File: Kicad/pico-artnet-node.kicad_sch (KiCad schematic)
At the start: 28 parts, among them J1 Conn_01x03_Pin, J2 Conn_01x03_Pin, J3 Conn_01x04_Pin, J4 Conn_01x05_Pin, J5 Conn_01x05_Pin, J6 Conn_01x02_Socket, J7 Conn_01x02_Socket, SW1 SW_SPST, SW2 SW_SPST, SW3 SW_SPST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

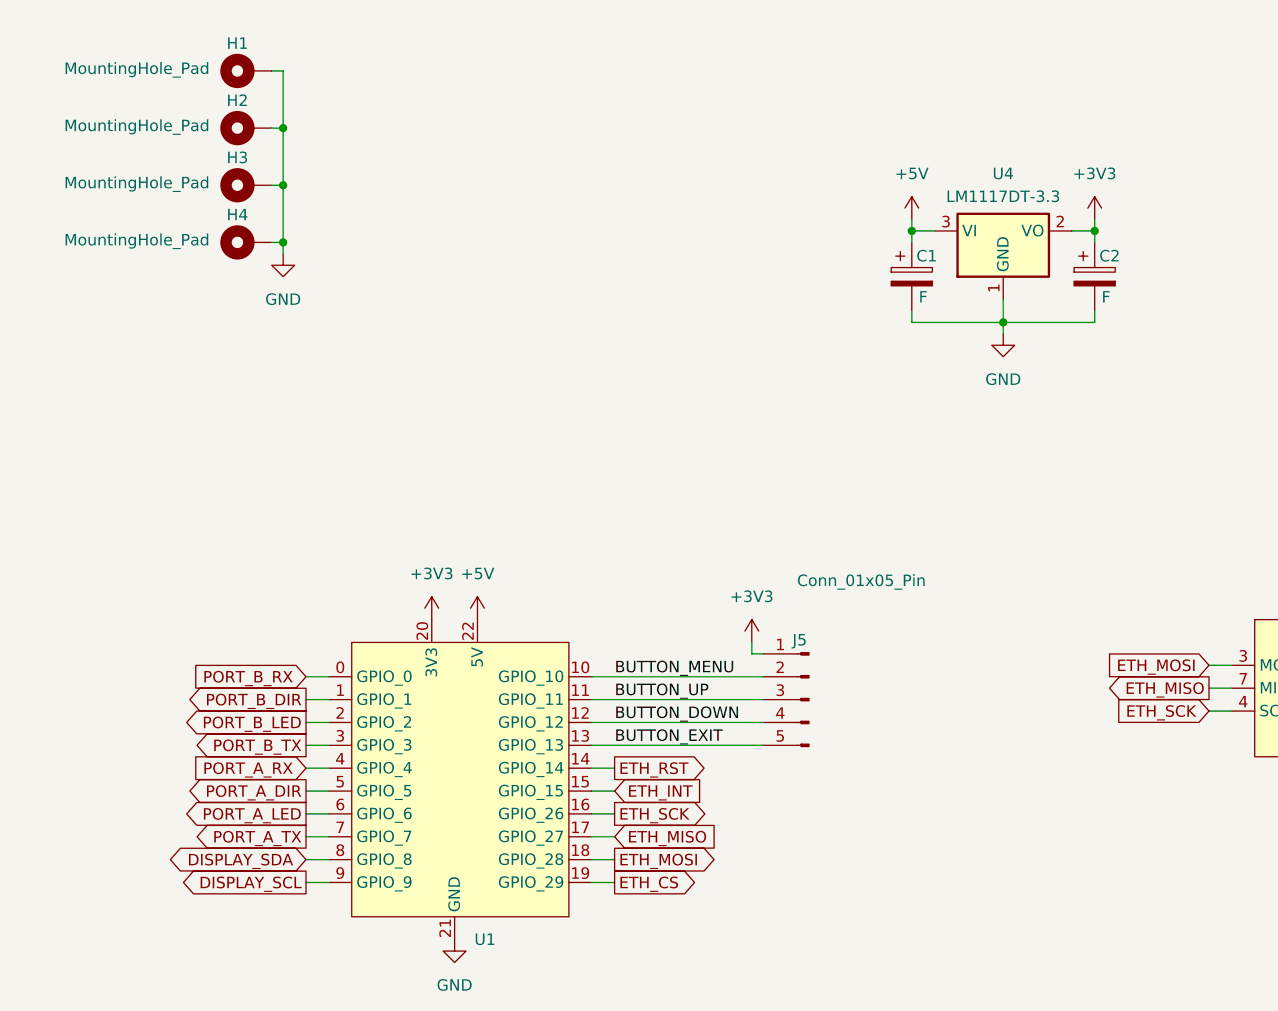
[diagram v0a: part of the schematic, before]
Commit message: swapped tx and led pins for better pcb layout
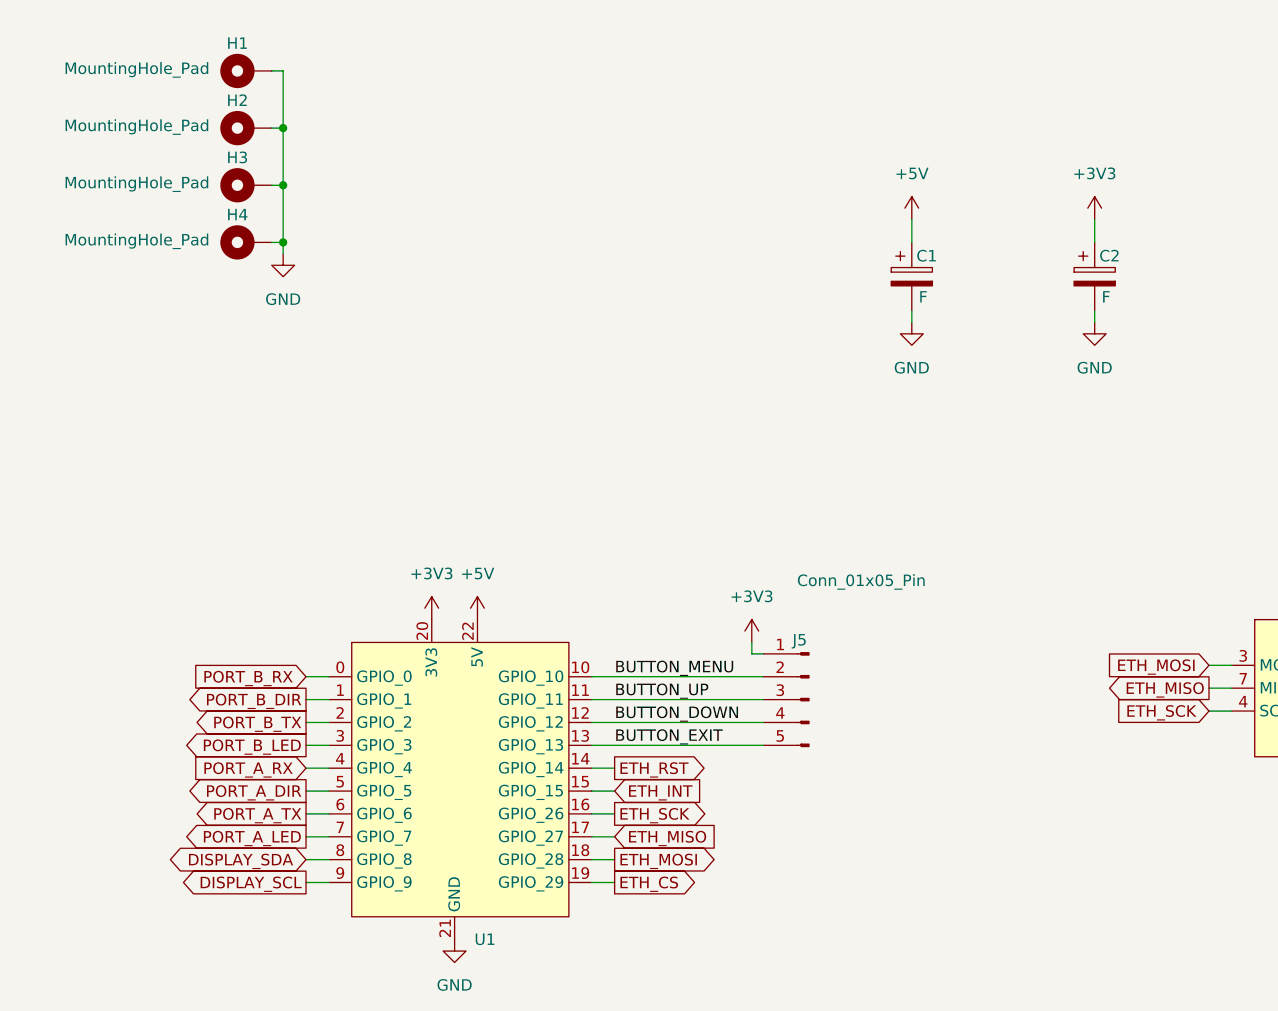
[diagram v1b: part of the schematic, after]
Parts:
- removed U4: LM1117DT-3.3, Package_TO_SOT_THT:TO-220-3_Vertical, symbol Regulator_Linear:LM1117DT-3.3
- R1, R2, R3, R4: footprint Resistor_THT:R_Axial_DIN0207_L6.3mm_D2.5mm_P10.16mm_Horizontal -> Resistor_THT:R_Axial_DIN0207_L6.3mm_D2.5mm_P2.54mm_Vertical
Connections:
- net PORT_A_LED: now also U1.7 (GPIO_7); no longer U1.6 (GPIO_6)
- net PORT_A_TX: now also U1.6 (GPIO_6); no longer U1.7 (GPIO_7)
- net PORT_B_LED: now also U1.3 (GPIO_3); no longer U1.2 (GPIO_2)
- net PORT_B_TX: now also U1.2 (GPIO_2); no longer U1.3 (GPIO_3)

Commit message: finished pcb
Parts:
- added SYM2: Logo_Open_Hardware_Small, Symbol:OSHW-Logo2_14.6x12mm_SilkScreen, symbol Graphic:Logo_Open_Hardware_Small
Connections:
- net at R2.1, U3.6 (A): now also J2.2 (Pin_2); no longer J2.3 (Pin_3)
- net at R2.2, U3.7 (B): now also J2.3 (Pin_3); no longer J2.2 (Pin_2)
- net at R1.1, U2.6 (A): now also J1.2 (Pin_2); no longer J1.3 (Pin_3)
- net at R1.2, U2.7 (B): now also J1.3 (Pin_3); no longer J1.2 (Pin_2)
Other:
- moved on the sheet: J1, J2
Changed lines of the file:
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@@
 	(wire
 		(pts
+			(xy 245.11 25.4) (xy 246.38 25.4)
+		)
+		(stroke
+			(width 0)
+			(type default)
+		)
+	)
+	(wire
+		(pts
 			(xy 63.5 182.88) (xy 63.5 173.99)
 		)
@@
 	(wire
 		(pts
-			(xy 246.38 74.93) (xy 245.11 74.93)
+			(xy 245.11 67.31) (xy 246.38 67.31)
 		)
 		(stroke
@@
 	(wire
 		(pts
-			(xy 41.91 109.22) (xy 44.45 109.22)
+			(xy 245.11 34.29) (xy 245.11 25.4)
 		)
 		(stroke
@@
 	(wire
 		(pts
-			(xy 73.66 91.44) (xy 92.71 91.44)
+			(xy 41.91 109.22) (xy 44.45 109.22)
 		)
 		(stroke
@@
 	(wire
 		(pts
-			(xy 81.28 185.42) (xy 81.28 173.99)
+			(xy 73.66 91.44) (xy 92.71 91.44)
 		)
 		(stroke
@@
 	(wire
 		(pts
-			(xy 87.63 173.99) (xy 86.36 173.99)
+			(xy 81.28 185.42) (xy 81.28 173.99)
 		)
 		(stroke
@@
 	(wire
 		(pts
-			(xy 215.9 34.29) (xy 214.63 34.29)
+			(xy 87.63 173.99) (xy 86.36 173.99)
 		)
 		(stroke
@@
 	(wire
 		(pts
-			(xy 41.91 106.68) (xy 44.45 106.68)
+			(xy 215.9 34.29) (xy 214.63 34.29)
 		)
 		(stroke
@@
 	(wire
 		(pts
-			(xy 237.49 31.75) (xy 236.22 31.75)
+			(xy 41.91 106.68) (xy 44.45 106.68)
 		)
 		(stroke
@@
 	(wire
 		(pts
-			(xy 142.24 179.07) (xy 139.7 179.07)
+			(xy 237.49 31.75) (xy 236.22 31.75)
 		)
 		(stroke
@@
 	(wire
 		(pts
-			(xy 246.38 33.02) (xy 245.11 33.02)
+			(xy 142.24 179.07) (xy 139.7 179.07)
 		)
 		(stroke
@@
 	(wire
 		(pts
-			(xy 245.11 74.93) (xy 245.11 76.2)
-		)
-		(stroke
-			(width 0)
-			(type default)
-		)
-	)
-	(wire
-		(pts
 			(xy 27.94 180.34) (xy 45.72 180.34)
 		)
@@
 	(wire
 		(pts
-			(xy 245.11 33.02) (xy 245.11 34.29)
-		)
-		(stroke
-			(width 0)
-			(type default)
-		)
-	)
-	(wire
-		(pts
 			(xy 73.66 88.9) (xy 92.71 88.9)
 		)
@@
 	(wire
 		(pts
+			(xy 245.11 76.2) (xy 245.11 67.31)
+		)
+		(stroke
+			(width 0)
+			(type default)
+		)
+	)
+	(wire
+		(pts
 			(xy 240.03 74.93) (xy 243.84 74.93)
 		)
@@
 	(symbol
 		(lib_id "Connector:Conn_01x03_Pin")
-		(at 251.46 72.39 180)
+		(at 251.46 69.85 0)
+		(mirror y)
 		(unit 1)
 		(exclude_from_sim no)
@@
 		(dnp no)
 		(property "Reference" "J2"
-			(at 250.825 80.01 0)
+			(at 250.825 62.23 0)
 			(effects
 				(font
@@
 		)
 		(property "Value" "Conn_01x03_Pin"
-			(at 261.366 79.248 0)
+			(at 261.366 62.992 0)
 			(effects
 				(font
@@
 		)
 		(property "Footprint" "Connector_PinHeader_2.54mm:PinHeader_1x03_P2.54mm_Vertical"
-			(at 251.46 72.39 0)
+			(at 251.46 69.85 0)
 			(effects
 				(font
@@
 		)
 		(property "Datasheet" "~"
-			(at 251.46 72.39 0)
+			(at 251.46 69.85 0)
 			(effects
 				(font
@@
 		)
 		(property "Description" "Generic connector, single row, 01x03, script generated"
-			(at 251.46 72.39 0)
+			(at 251.46 69.85 0)
 			(effects
 				(font
@@
 	)
 	(symbol
+		(lib_id "Graphic:Logo_Open_Hardware_Small")
+		(at 166.37 140.97 0)
+		(unit 1)
+		(exclude_from_sim yes)
+		(in_bom no)
+		(on_board yes)
+		(dnp no)
+		(fields_autoplaced yes)
+		(property "Reference" "SYM2"
+			(at 166.37 133.985 0)
+			(effects
+				(font
+					(size 1.27 1.27)
+				)
+				(hide yes)
+			)
+		)
+		(property "Value" "Logo_Open_Hardware_Small"
+			(at 166.37 146.685 0)
+			(effects
+				(font
+					(size 1.27 1.27)
+				)
+				(hide yes)
+			)
+		)
+		(property "Footprint" "Symbol:OSHW-Logo2_14.6x12mm_SilkScreen"
+			(at 166.37 140.97 0)
+			(effects
+				(font
+					(size 1.27 1.27)
+				)
+				(hide yes)
+			)
+		)
+		(property "Datasheet" "~"
+			(at 166.37 140.97 0)
+			(effects
+				(font
+					(size 1.27 1.27)
+				)
+				(hide yes)
+			)
+		)
+		(property "Description" "Open Hardware logo, small"
+			(at 166.37 140.97 0)
+			(effects
+				(font
+					(size 1.27 1.27)
+				)
+				(hide yes)
+			)
+		)
+		(instances
+			(project ""
+				(path "/7b0a91fa-c31e-43bb-b474-f9fdc8ba9323"
+					(reference "SYM2")
+					(unit 1)
+				)
+			)
+		)
+	)
+	(symbol
 		(lib_id "power:+3V3")
 		(at 226.06 120.65 0)
@@
 	(symbol
 		(lib_id "Connector:Conn_01x03_Pin")
-		(at 251.46 30.48 180)
+		(at 251.46 27.94 0)
+		(mirror y)
 		(unit 1)
 		(exclude_from_sim no)
@@
 		(dnp no)
 		(property "Reference" "J1"
-			(at 250.825 38.1 0)
+			(at 250.825 20.32 0)
 			(effects
 				(font
@@
 		)
 		(property "Value" "Conn_01x03_Pin"
-			(at 259.588 38.608 0)
+			(at 259.588 19.812 0)
 			(effects
 				(font
@@
 		)
 		(property "Footprint" "Connector_PinHeader_2.54mm:PinHeader_1x03_P2.54mm_Vertical"
-			(at 251.46 30.48 0)
+			(at 251.46 27.94 0)
 			(effects
 				(font
@@
 		)
 		(property "Datasheet" "~"
-			(at 251.46 30.48 0)
+			(at 251.46 27.94 0)
 			(effects
 				(font
@@
 		)
 		(property "Description" "Generic connector, single row, 01x03, script generated"
-			(at 251.46 30.48 0)
+			(at 251.46 27.94 0)
 			(effects
 				(font

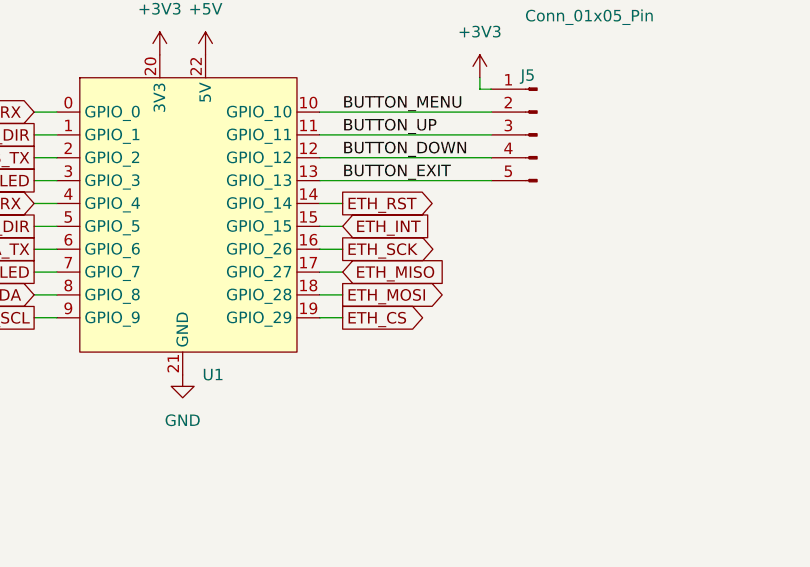
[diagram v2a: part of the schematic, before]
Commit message: swapped miso and mosi lines so they connect correctly
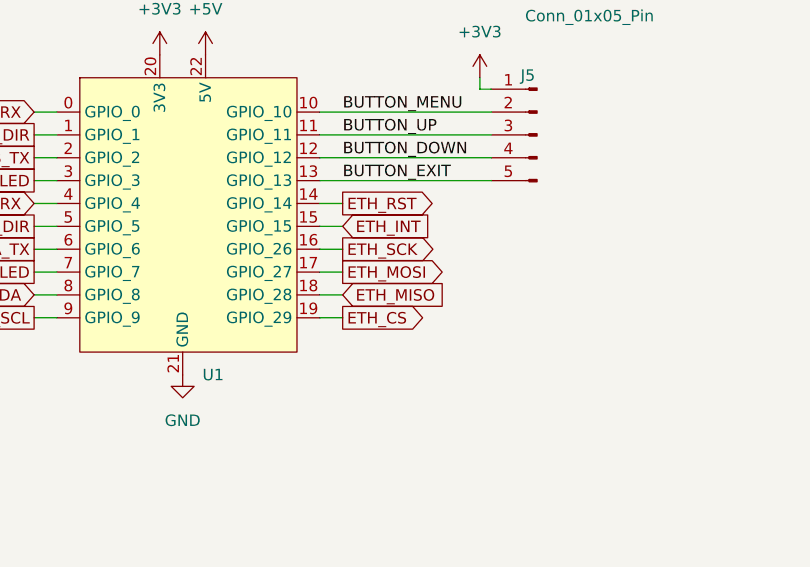
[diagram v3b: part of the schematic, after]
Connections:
- net ETH_MISO: now also U1.18 (GPIO_28); no longer U1.17 (GPIO_27)
- net ETH_MOSI: now also U1.17 (GPIO_27); no longer U1.18 (GPIO_28)
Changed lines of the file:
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@@
 	(global_label "ETH_MOSI"
 		(shape output)
-		(at 76.2 106.68 0)
-		(fields_autoplaced yes)
-		(effects
-			(font
-				(size 1.27 1.27)
-			)
-			(justify left)
-		)
-		(property "Intersheetrefs" "${INTERSHEET_REFS}"
-			(at 88.1961 106.68 0)
+		(at 76.2 104.14 0)
+		(fields_autoplaced yes)
+		(effects
+			(font
+				(size 1.27 1.27)
+			)
+			(justify left)
+		)
+		(property "Intersheetrefs" "${INTERSHEET_REFS}"
+			(at 88.1961 104.14 0)
 			(effects
 				(font
@@
 	(global_label "ETH_MISO"
 		(shape input)
-		(at 76.2 104.14 0)
-		(fields_autoplaced yes)
-		(effects
-			(font
-				(size 1.27 1.27)
-			)
-			(justify left)
-		)
-		(property "Intersheetrefs" "${INTERSHEET_REFS}"
-			(at 88.1961 104.14 0)
-			(effects
-				(font
+		(at 76.2 106.68 0)
+		(fields_autoplaced yes)
+		(effects
+			(font
+				(size 1.27 1.27)
+			)
+			(justify left)
+		)
+		(property "Intersheetrefs" "${INTERSHEET_REFS}"
+			(at 88.1961 106.68 0)
+			(effects
+				(font
